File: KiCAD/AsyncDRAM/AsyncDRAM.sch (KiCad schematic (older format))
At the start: 14 parts, among them J1 UART, J2 SPI, J3 UPDI, J4 POWER

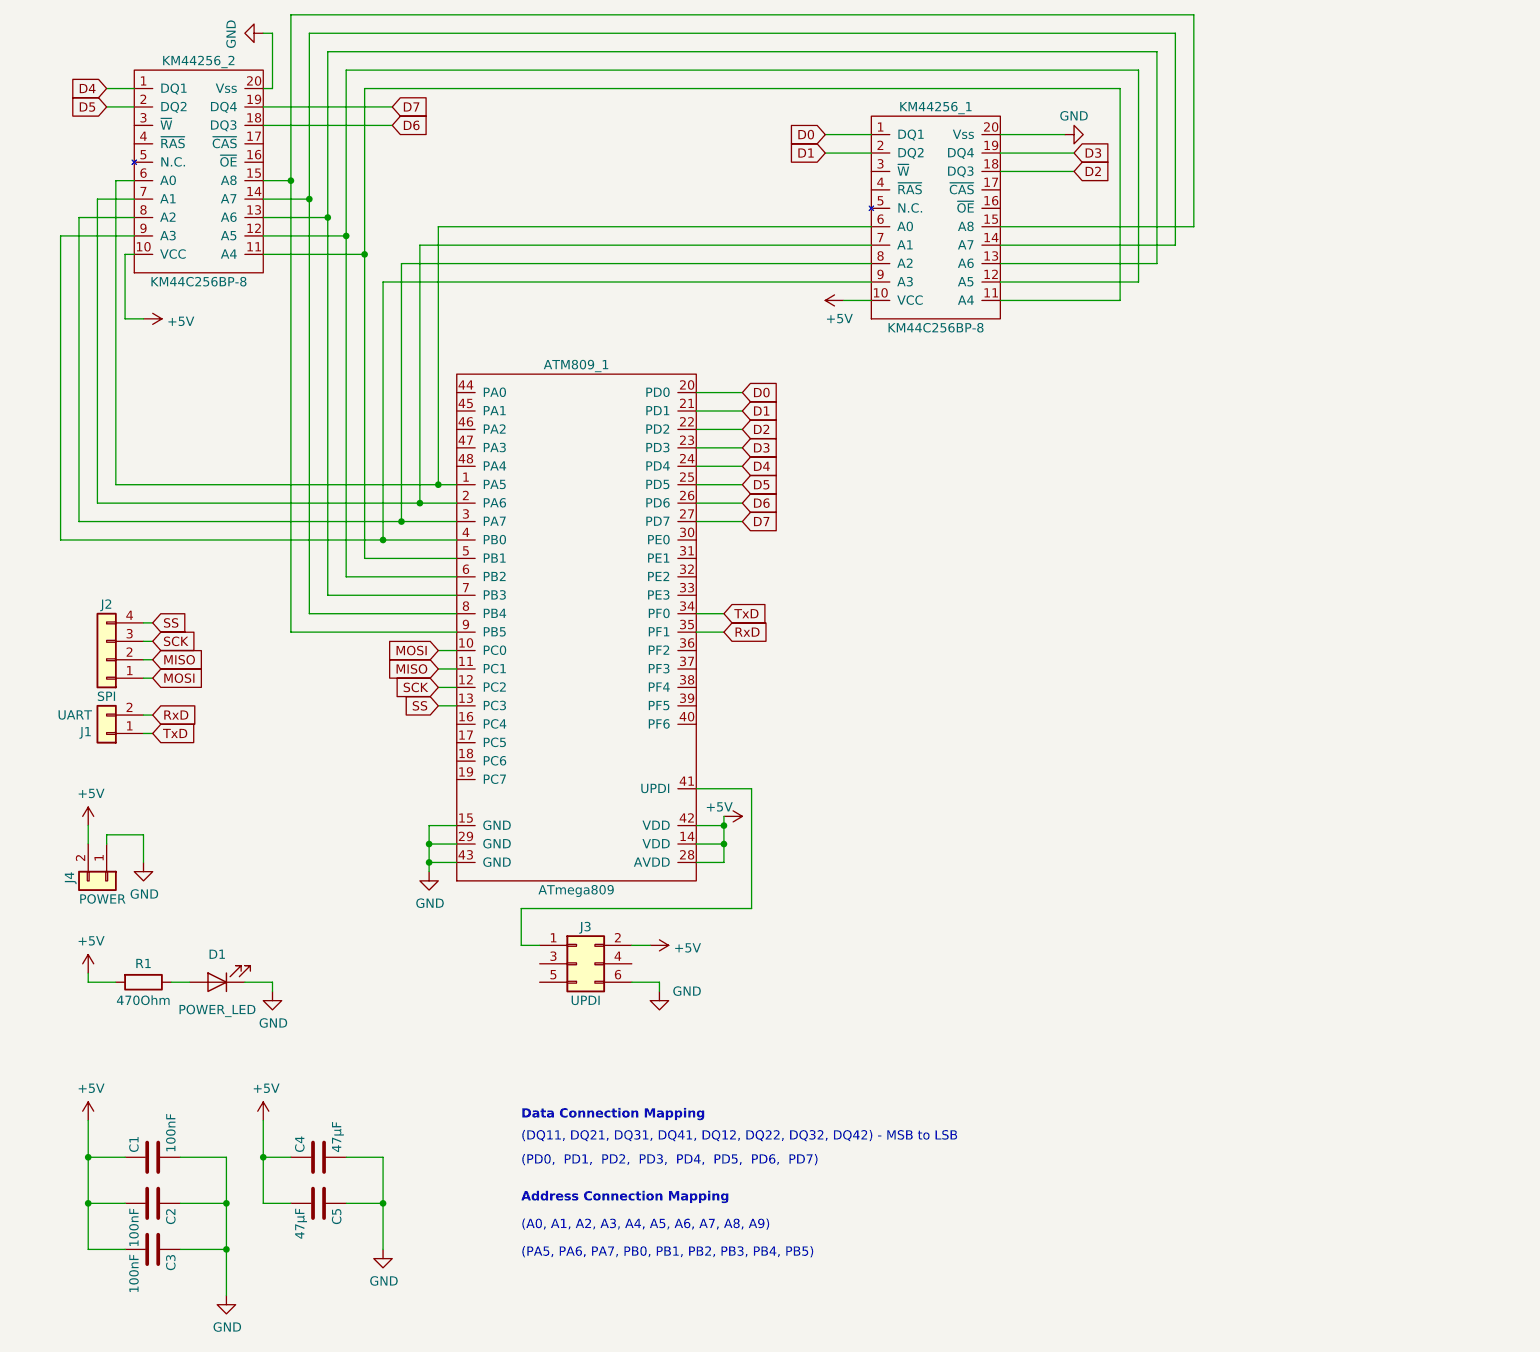
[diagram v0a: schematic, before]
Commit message: Finalizing schematic, adding TQFP footprint, PCB outline
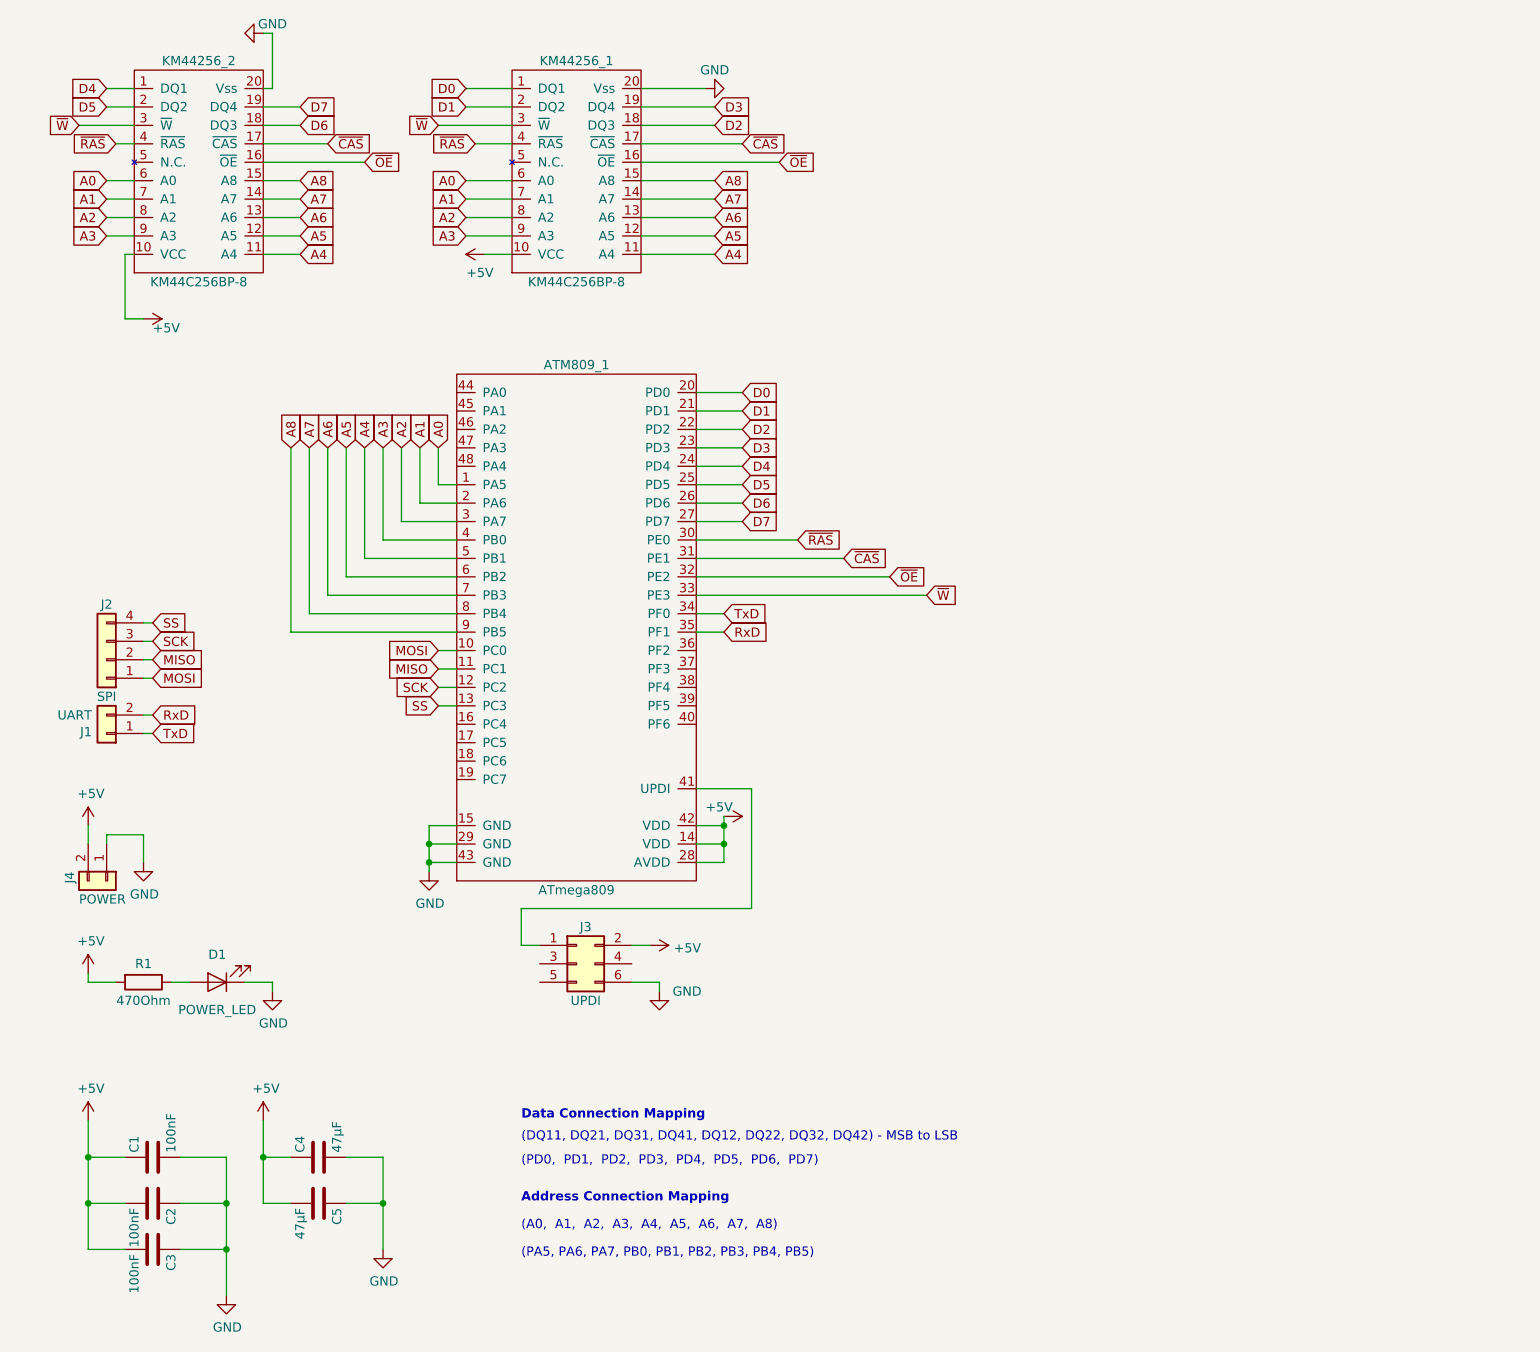
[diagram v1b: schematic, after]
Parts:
- ATM809_1: footprint (none) -> QFP:TQFP-48_7x7mm_P0.5mm
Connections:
- net A4: now reaches ATM809_1.5 (PB1), KM44256_1.11 (A4), KM44256_2.11 (A4)
- net A5: now reaches ATM809_1.6 (PB2), KM44256_1.12 (A5), KM44256_2.12 (A5)
- net A6: now reaches ATM809_1.7 (PB3), KM44256_1.13 (A6), KM44256_2.13 (A6)
- net A7: now reaches ATM809_1.8 (PB4), KM44256_1.14 (A7), KM44256_2.14 (A7)
- net A8: now reaches ATM809_1.9 (PB5), KM44256_1.15 (A8), KM44256_2.15 (A8)
- net ~OE: now reaches KM44256_1.16 (~OE)
- net ~OE: now also ATM809_1.32 (PE2), KM44256_2.16 (~OE)
- net ~CAS: now reaches KM44256_1.17 (~CAS)
- net ~CAS: now also ATM809_1.31 (PE1), KM44256_2.17 (~CAS)
- net ~W: now reaches KM44256_1.3 (~W)
- net ~W: now also ATM809_1.33 (PE3), KM44256_2.3 (~W)
- net ~RAS: now reaches KM44256_1.4 (~RAS)
- net ~RAS: now also ATM809_1.30 (PE0), KM44256_2.4 (~RAS)
- net A0: now reaches ATM809_1.1 (PA5), KM44256_1.6 (A0), KM44256_2.6 (A0)
- net A1: now reaches ATM809_1.2 (PA6), KM44256_1.7 (A1), KM44256_2.7 (A1)
- net A2: now reaches ATM809_1.3 (PA7), KM44256_1.8 (A2), KM44256_2.8 (A2)
- net A3: now reaches ATM809_1.4 (PB0), KM44256_1.9 (A3), KM44256_2.9 (A3)
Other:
- note added: "(A0, A1, A2, A3, A4, A5, A6, A7, A8)"
- note removed: "(A0, A1, A2, A3, A4, A5, A6, A7, A8, A9)"
- moved on the sheet: KM44256_1

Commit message: Adjusted board settings to Elecrow Specifications
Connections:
- net +5V: now also D1.2 (A); no longer R1.2
- net GND: now also R1.1; no longer D1.1 (K)
- net UPDI: now reaches ATM809_1.41 (UPDI), J3.1 (Pin_1)
- new net: D1.1 (K), R1.2
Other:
- moved on the sheet: D1, R1
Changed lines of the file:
@@
 L Device:LED D1
 U 1 1 5DADF535
-P 1350 5750
-F 0 "D1" H 1350 5600 50  0000 C CNN
-F 1 "POWER_LED" H 1350 5900 50  0000 C CNN
-F 2 "LEDSMD:LED_1206_3216Metric" H 1350 5750 50  0001 C CNN
-F 3 "~" H 1350 5750 50  0001 C CNN
-	1    1350 5750
+P 1050 5750
+F 0 "D1" H 1050 5600 50  0000 C CNN
+F 1 "POWER_LED" H 1050 5900 50  0000 C CNN
+F 2 "LEDSMD:LED_1206_3216Metric" H 1050 5750 50  0001 C CNN
+F 3 "~" H 1050 5750 50  0001 C CNN
+	1    1050 5750
 	-1   0    0    1
 $EndComp
@@
 L Power:GND #PWR0112
 U 1 1 5DAE0D3A
-P 1650 5800
-F 0 "#PWR0112" H 1650 5550 50  0001 C CNN
-F 1 "GND" H 1655 5627 50  0000 C CNN
-F 2 "" H 1650 5800 50  0001 C CNN
-F 3 "" H 1650 5800 50  0001 C CNN
-	1    1650 5800
-	1    0    0    -1
-$EndComp
-Wire Wire Line
-	1650 5750 1650 5800
-Wire Wire Line
-	1200 5750 1100 5750
+P 1600 5800
+F 0 "#PWR0112" H 1600 5550 50  0001 C CNN
+F 1 "GND" H 1605 5627 50  0000 C CNN
+F 2 "" H 1600 5800 50  0001 C CNN
+F 3 "" H 1600 5800 50  0001 C CNN
+	1    1600 5800
+	1    0    0    -1
+$EndComp
 Wire Wire Line
 	1750 3850 2650 3850
@@
 	-1   0    0    1
 $EndComp
-Wire Wire Line
-	1500 5750 1650 5750
 $Comp
 L Connectors_Generic:Conn_02x03_Odd_Even J3
@@
 	1    0    0    -1
 $EndComp
-Wire Wire Line
-	3950 4700 4250 4700
-Wire Wire Line
-	4250 4700 4250 5350
-Wire Wire Line
-	4250 5350 3000 5350
-Wire Wire Line
-	3000 5350 3000 5550
-Wire Wire Line
-	3000 5550 3100 5550
 $Comp
 L Power:+5V #PWR0113
@@
 L Device:R R1
 U 1 1 5DD94764
-P 950 5750
-F 0 "R1" V 850 5750 50  0000 C CNN
-F 1 "470Ohm" V 1050 5750 50  0000 C CNN
-F 2 "ResistorSMD:R_0805_2012Metric" V 880 5750 50  0001 C CNN
-F 3 "~" H 950 5750 50  0001 C CNN
-	1    950  5750
+P 1400 5750
+F 0 "R1" V 1300 5750 50  0000 C CNN
+F 1 "470Ohm" V 1500 5750 50  0000 C CNN
+F 2 "ResistorSMD:R_0805_2012Metric" V 1330 5750 50  0001 C CNN
+F 3 "~" H 1400 5750 50  0001 C CNN
+	1    1400 5750
 	0    1    1    0
 $EndComp
-Wire Wire Line
-	800  5750 650  5750
 Wire Wire Line
 	650  5750 650  5700
@@
 Wire Wire Line
 	4400 1300 3650 1300
+Wire Wire Line
+	1200 5750 1250 5750
+Wire Wire Line
+	1550 5750 1600 5750
+Wire Wire Line
+	1600 5750 1600 5800
+Wire Wire Line
+	650  5750 900  5750
+Text GLabel 3000 5550 0    50   Input ~ 0
+UPDI
+Wire Wire Line
+	3000 5550 3100 5550
+Text GLabel 4100 4700 2    50   Input ~ 0
+UPDI
+Wire Wire Line
+	4100 4700 3950 4700
 $EndSCHEMATC

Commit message: Fixed LED finally
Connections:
- net +5V: now also R1.2; no longer D1.2 (A)
- net GND: now also D1.1 (K); no longer R1.1
- new net: D1.2 (A), R1.1
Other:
- moved on the sheet: D1, R1
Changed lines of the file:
@@
 L Device:LED D1
 U 1 1 5DADF535
-P 1050 5750
-F 0 "D1" H 1050 5600 50  0000 C CNN
-F 1 "POWER_LED" H 1050 5900 50  0000 C CNN
-F 2 "LEDSMD:LED_1206_3216Metric" H 1050 5750 50  0001 C CNN
-F 3 "~" H 1050 5750 50  0001 C CNN
-	1    1050 5750
+P 1300 5750
+F 0 "D1" H 1300 5600 50  0000 C CNN
+F 1 "POWER_LED" H 1300 5900 50  0000 C CNN
+F 2 "LEDSMD:LED_1206_3216Metric" H 1300 5750 50  0001 C CNN
+F 3 "~" H 1300 5750 50  0001 C CNN
+	1    1300 5750
 	-1   0    0    1
 $EndComp
@@
 L Device:R R1
 U 1 1 5DD94764
-P 1400 5750
-F 0 "R1" V 1300 5750 50  0000 C CNN
-F 1 "470Ohm" V 1500 5750 50  0000 C CNN
-F 2 "ResistorSMD:R_0805_2012Metric" V 1330 5750 50  0001 C CNN
-F 3 "~" H 1400 5750 50  0001 C CNN
-	1    1400 5750
+P 900 5750
+F 0 "R1" V 800 5750 50  0000 C CNN
+F 1 "470Ohm" V 1000 5750 50  0000 C CNN
+F 2 "ResistorSMD:R_0805_2012Metric" V 830 5750 50  0001 C CNN
+F 3 "~" H 900 5750 50  0001 C CNN
+	1    900  5750
 	0    1    1    0
 $EndComp
-Wire Wire Line
-	650  5750 650  5700
 Text Notes 3000 7250 0    50   ~ 0
 (PA5, PA6, PA7, PB0, PB1, PB2, PB3, PB4, PB5)
@@
 Wire Wire Line
 	4400 1300 3650 1300
-Wire Wire Line
-	1200 5750 1250 5750
-Wire Wire Line
-	1550 5750 1600 5750
-Wire Wire Line
-	1600 5750 1600 5800
-Wire Wire Line
-	650  5750 900  5750
 Text GLabel 3000 5550 0    50   Input ~ 0
 UPDI
@@
 Wire Wire Line
 	4100 4700 3950 4700
+Wire Wire Line
+	1050 5750 1150 5750
+Wire Wire Line
+	750  5750 650  5750
+Wire Wire Line
+	650  5750 650  5700
+Wire Wire Line
+	1450 5750 1600 5750
+Wire Wire Line
+	1600 5750 1600 5800
 $EndSCHEMATC

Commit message: Update Praesi
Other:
- note removed: "(A0, A1, A2, A3, A4, A5, A6, A7, A8)"
- note removed: "(DQ11, DQ21, DQ31, DQ41, DQ12, DQ22, DQ32, DQ42) - MSB to LSB\n\n"
- note removed: "(PA5, PA6, PA7, PB0, PB1, PB2, PB3, PB4, PB5)"
- note removed: "(PD0, PD1, PD2, PD3, PD4, PD5, PD6, PD7)"
- note removed: "Address Connection Mapping"
- note removed: "Data Connection Mapping"
- moved on the sheet: ATM809_1, C1, C2, C3, C4, C5, D1, J1, J2, J3, J4, R1
